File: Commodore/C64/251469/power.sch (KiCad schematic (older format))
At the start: 11 parts, among them CN10 LED Connector, CN7 Power Input, SW1 Power Switch

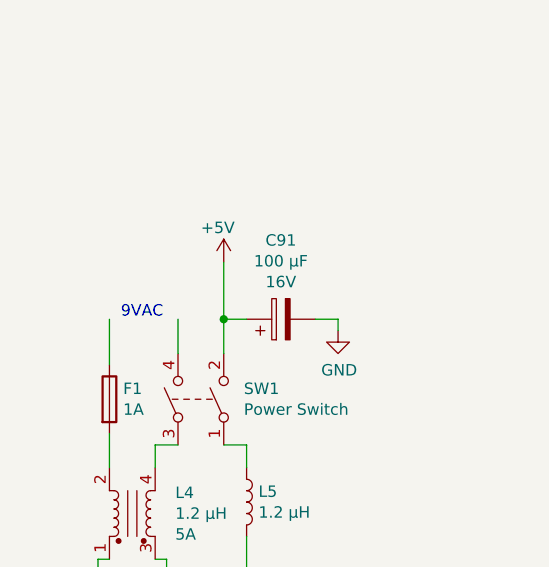
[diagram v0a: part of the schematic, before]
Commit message: Using new 9VAC power symbol
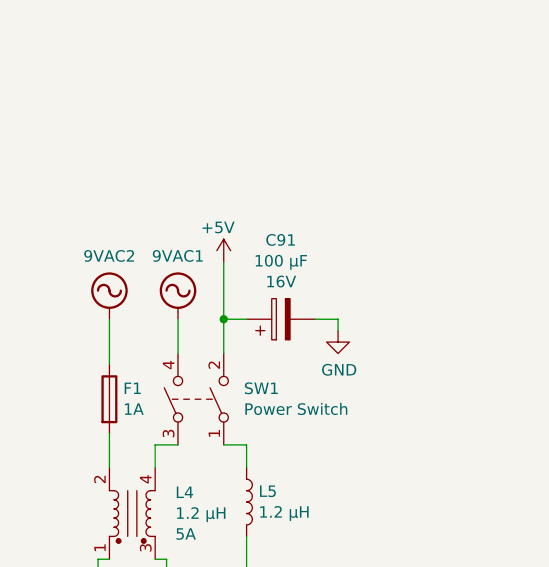
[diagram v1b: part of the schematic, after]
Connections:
- net labels added: 9VAC1, 9VAC2
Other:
- note removed: "9VAC"
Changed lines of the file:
@@
 Wire Wire Line
 	1300 4550 1300 4700
-Text Notes 1050 4550 0    50   ~ 0
-9VAC
+$Comp
+L power_more:9VAC1 #PWR?
+U 1 1 5D2DC784
+P 1300 4550
+F 0 "#PWR?" H 1300 4450 50  0001 C CNN
+F 1 "9VAC1" H 1300 4825 50  0000 C CNN
+F 2 "" H 1300 4550 50  0001 C CNN
+F 3 "" H 1300 4550 50  0001 C CNN
+	1    1300 4550
+	1    0    0    -1
+$EndComp
+$Comp
+L power_more:9VAC2 #PWR?
+U 1 1 5D2DE867
+P 1000 4550
+F 0 "#PWR?" H 1000 4450 50  0001 C CNN
+F 1 "9VAC2" H 1000 4825 50  0000 C CNN
+F 2 "" H 1000 4550 50  0001 C CNN
+F 3 "" H 1000 4550 50  0001 C CNN
+	1    1000 4550
+	1    0    0    -1
+$EndComp
 $EndSCHEMATC

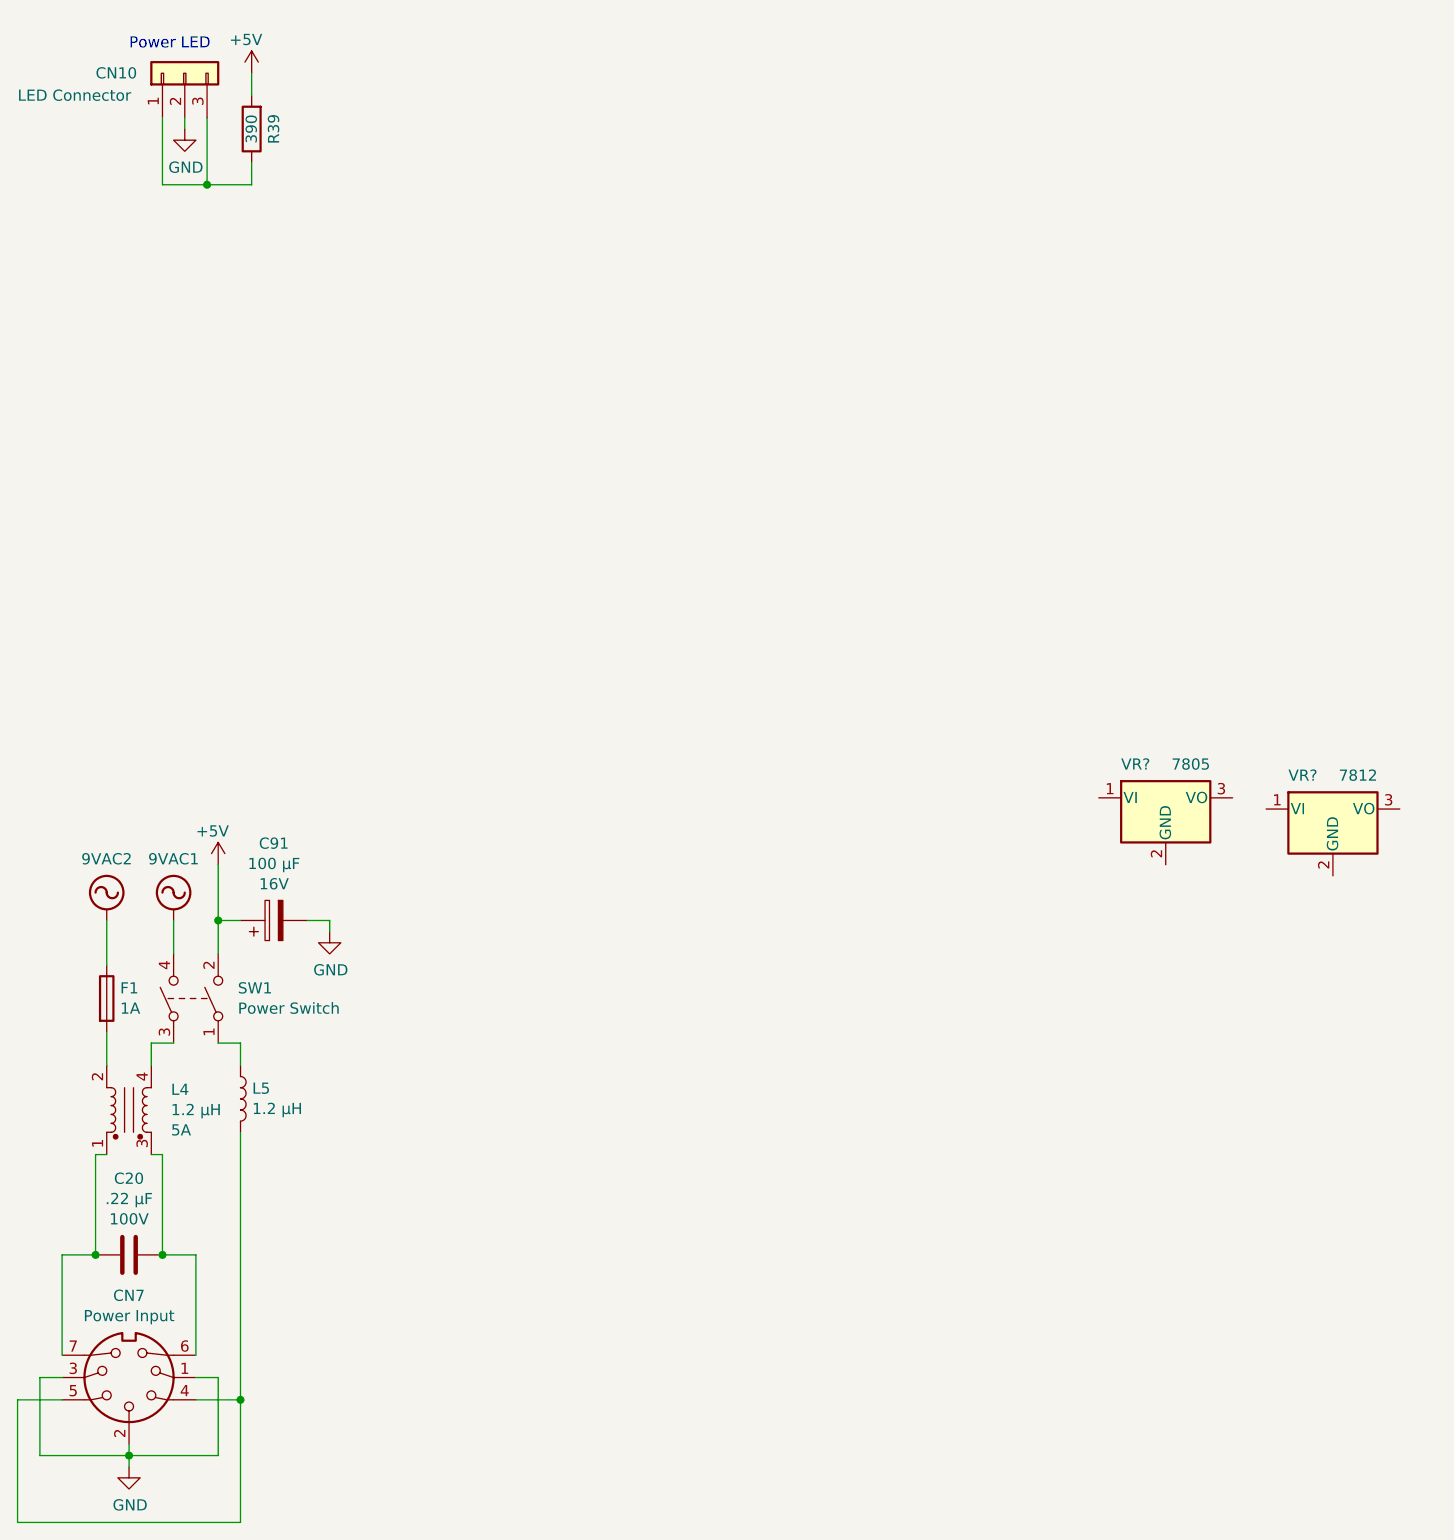
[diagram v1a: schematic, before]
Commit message: CAN+5V regulation circuit added
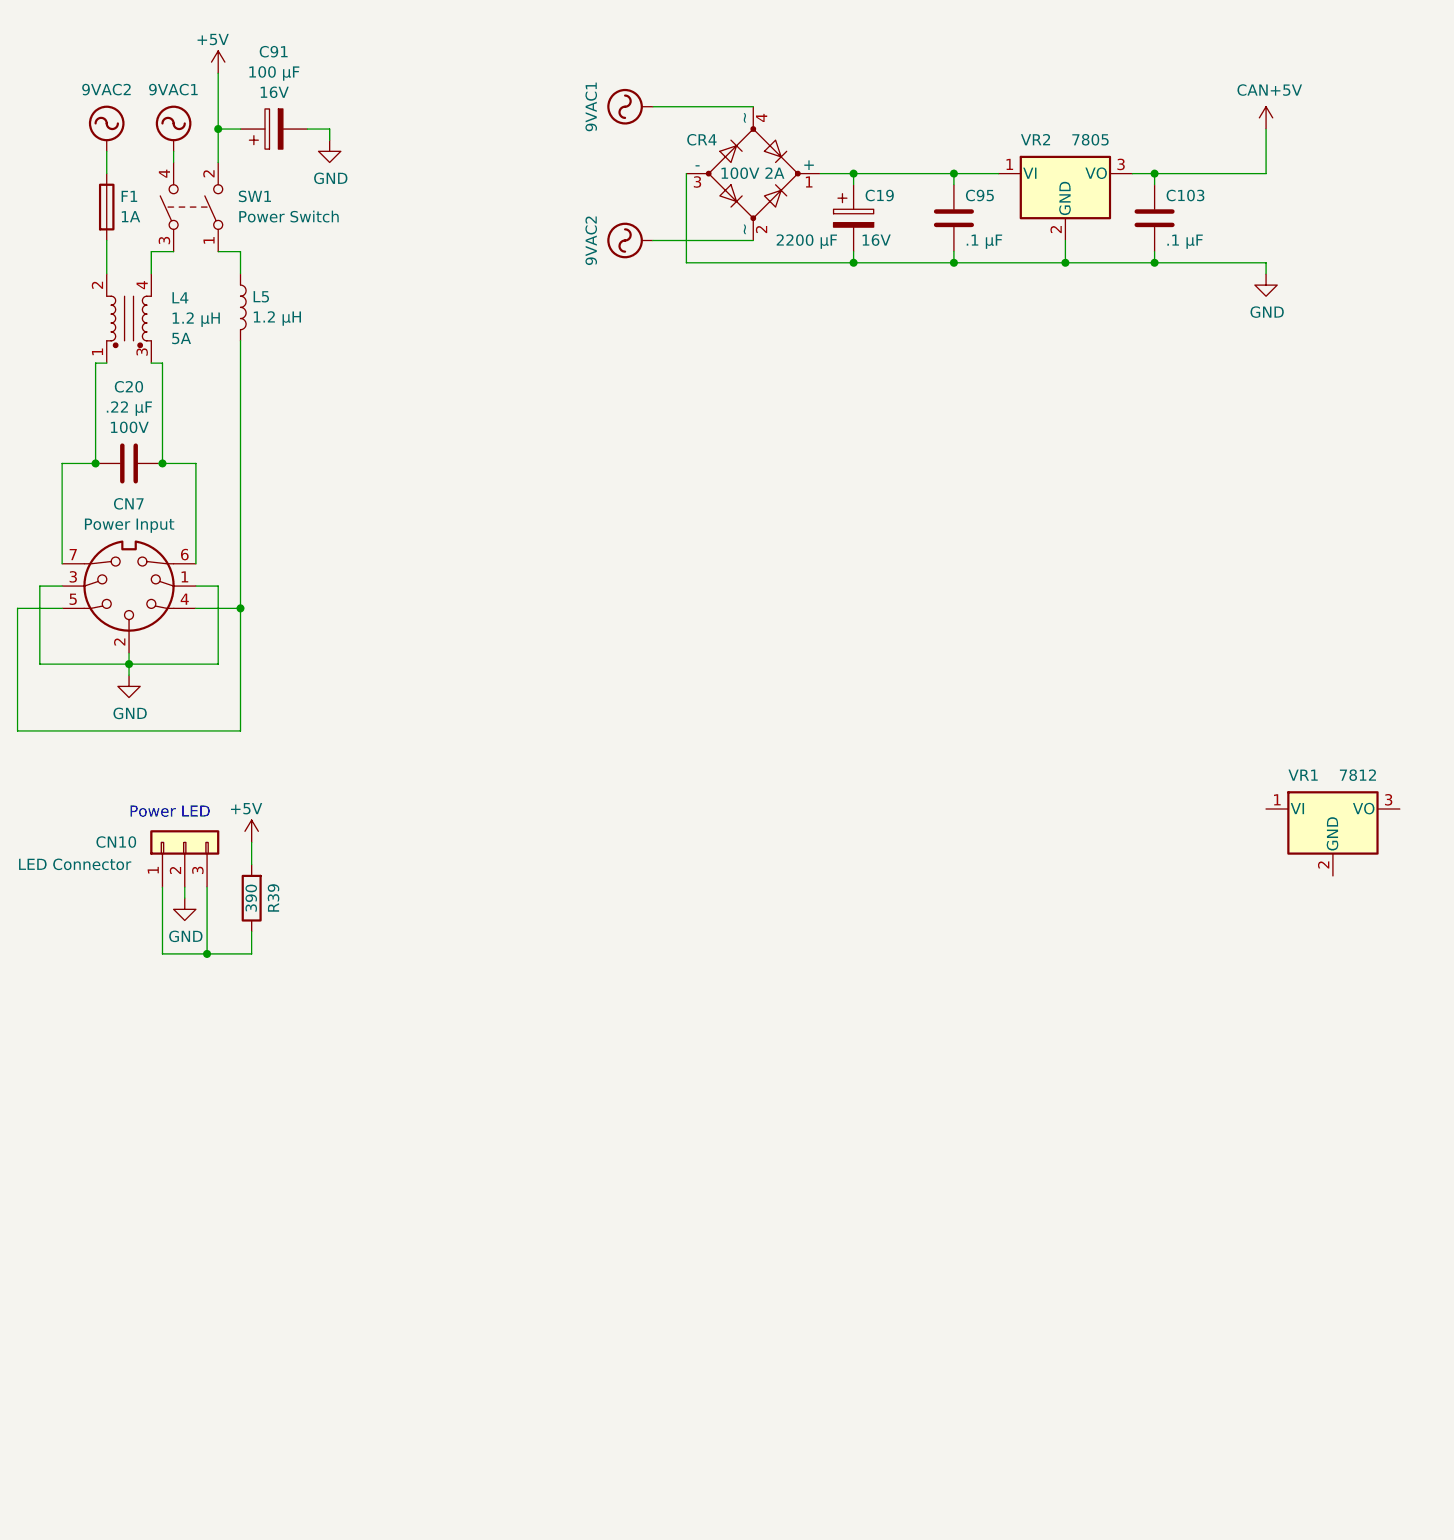
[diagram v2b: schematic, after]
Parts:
- added C103, C95: .1 μF, symbol Device:C
- added C19: 2200 μF, symbol Device:CP
- added CR4: 100V 2A, symbol Device:D_Bridge_+A-A
- gave numbers to parts that had none: 2
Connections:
- net +5V: now also VR2.3 (VO), C103.1
- net GND: now also VR2.2 (GND), C103.2, C19.2, C95.2, CR4.3 (-)
- net VAC: now also CR4.2 (~~), CR4.4 (~~)
- net at VR2.1 (VI): now also C19.1, C95.1, CR4.1 (+)
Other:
- moved on the sheet: C20, C91, CN10, CN7, F1, L4, L5, R39, SW1, VR2

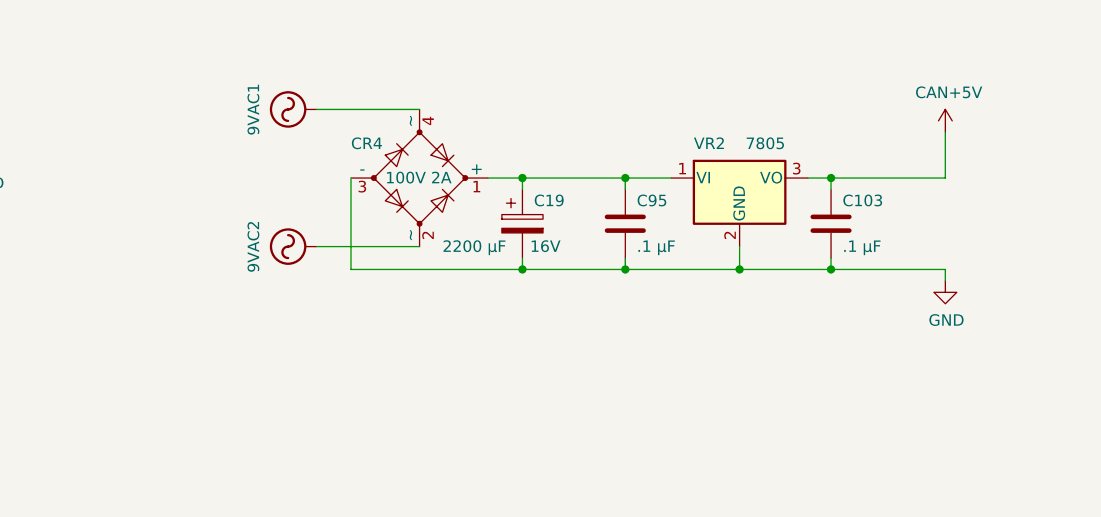
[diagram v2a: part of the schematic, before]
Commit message: UNREG+9V regulation circuit added
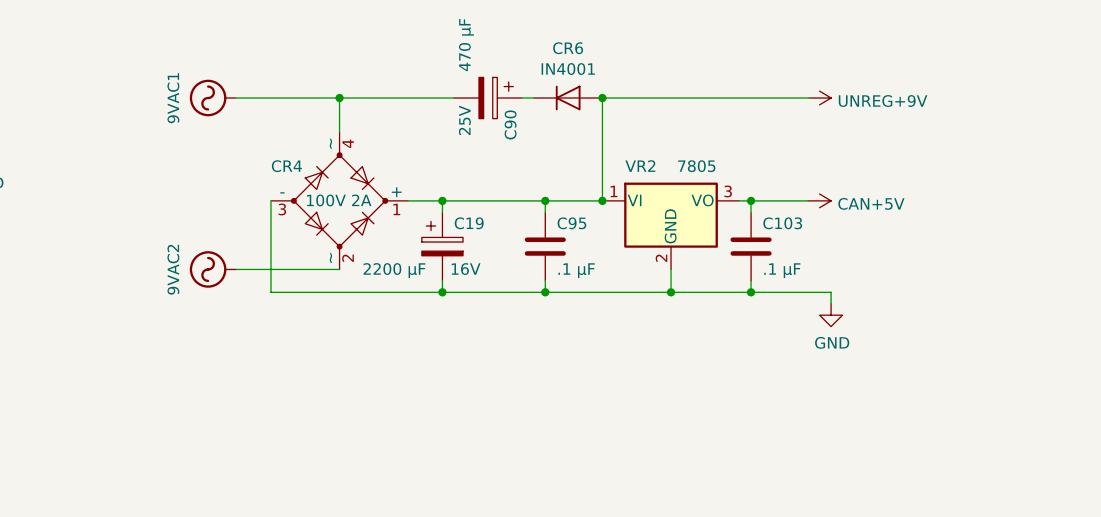
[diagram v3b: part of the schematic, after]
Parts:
- added C90: 470 μF, symbol Device:CP
- added CR6: IN4001, symbol Device:D
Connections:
- net VAC: now also C90.2
- net +9V: now reaches C19.1, C95.1, CR4.1 (+), VR2.1 (VI)
- net +9V: now also CR6.2 (A)
- new net: C90.1, CR6.1 (K)
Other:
- moved on the sheet: C103, C19, C95, CR4, VR2
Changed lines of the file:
@@
 L Regulator_Linear:LM7805_TO220 VR?
 U 1 1 5D95204B
-P 5300 1200
+P 5000 1300
 AR Path="/5D95204B" Ref="VR?"  Part="1"
 AR Path="/5D94F152/5D95204B" Ref="VR2"  Part="1"
-F 0 "VR2" H 5100 1350 50  0000 L CNN
-F 1 "7805" H 5500 1350 50  0000 R CNN
-F 2 "Package_TO_SOT_THT:TO-220-3_Vertical" H 5300 1425 50  0001 C CIN
-F 3 "http://www.fairchildsemi.com/ds/LM/LM7805.pdf" H 5300 1150 50  0001 C CNN
-	1    5300 1200
+F 0 "VR2" H 4800 1450 50  0000 L CNN
+F 1 "7805" H 5200 1450 50  0000 R CNN
+F 2 "Package_TO_SOT_THT:TO-220-3_Vertical" H 5000 1525 50  0001 C CIN
+F 3 "http://www.fairchildsemi.com/ds/LM/LM7805.pdf" H 5000 1250 50  0001 C CNN
+	1    5000 1300
 	1    0    0    -1
 $EndComp
@@
 L Device:D_Bridge_+A-A CR4
 U 1 1 5D30E6B0
-P 3900 1200
-F 0 "CR4" H 3600 1350 50  0000 L CNN
-F 1 "100V 2A" H 3750 1200 50  0000 L CNN
-F 2 "" H 3900 1200 50  0001 C CNN
-F 3 "~" H 3900 1200 50  0001 C CNN
-F 4 "100V" H 4100 1450 50  0001 C CNN "Voltage Rating"
-F 5 "2A" H 4200 1350 50  0001 C CNN "Current Rating"
-	1    3900 1200
+P 3550 1300
+F 0 "CR4" H 3250 1450 50  0000 L CNN
+F 1 "100V 2A" H 3400 1300 50  0000 L CNN
+F 2 "" H 3550 1300 50  0001 C CNN
+F 3 "~" H 3550 1300 50  0001 C CNN
+F 4 "100V" H 3750 1550 50  0001 C CNN "Voltage Rating"
+F 5 "2A" H 3850 1450 50  0001 C CNN "Current Rating"
+	1    3550 1300
 	1    0    0    -1
 $EndComp
@@
 L power_more:9VAC2 #PWR?
 U 1 1 5D30F39C
-P 3450 1500
-F 0 "#PWR?" H 3450 1400 50  0001 C CNN
-F 1 "9VAC2" H 3450 1775 50  0000 C CNN
-F 2 "" H 3450 1500 50  0001 C CNN
-F 3 "" H 3450 1500 50  0001 C CNN
-	1    3450 1500
+P 3100 1600
+F 0 "#PWR?" H 3100 1500 50  0001 C CNN
+F 1 "9VAC2" H 3100 1875 50  0000 C CNN
+F 2 "" H 3100 1600 50  0001 C CNN
+F 3 "" H 3100 1600 50  0001 C CNN
+	1    3100 1600
 	0    -1   -1   0
 $EndComp
@@
 L power_more:9VAC1 #PWR?
 U 1 1 5D30F3A6
-P 3450 900
-F 0 "#PWR?" H 3450 800 50  0001 C CNN
-F 1 "9VAC1" H 3450 1175 50  0000 C CNN
-F 2 "" H 3450 900 50  0001 C CNN
-F 3 "" H 3450 900 50  0001 C CNN
-	1    3450 900
-	0    -1   -1   0
-$EndComp
-Wire Wire Line
-	3900 900  3450 900
-Wire Wire Line
-	3900 1500 3450 1500
-Wire Wire Line
-	3600 1200 3600 1600
-Wire Wire Line
-	3600 1600 4350 1600
+P 3100 850
+F 0 "#PWR?" H 3100 750 50  0001 C CNN
+F 1 "9VAC1" H 3100 1125 50  0000 C CNN
+F 2 "" H 3100 850 50  0001 C CNN
+F 3 "" H 3100 850 50  0001 C CNN
+	1    3100 850
+	0    -1   -1   0
+$EndComp
+Wire Wire Line
+	3250 1300 3250 1700
+Wire Wire Line
+	3250 1700 4000 1700
 $Comp
 L Device:CP C19
 U 1 1 5D319DAB
-P 4350 1400
-F 0 "C19" H 4400 1500 50  0000 L CNN
-F 1 "2200 μF" H 4000 1300 50  0000 L CNN
-F 2 "" H 4388 1250 50  0001 C CNN
-F 3 "~" H 4350 1400 50  0001 C CNN
-F 4 "16V" H 4450 1300 50  0000 C CNN "Voltage Rating"
-	1    4350 1400
-	1    0    0    -1
-$EndComp
-Wire Wire Line
-	4350 1550 4350 1600
-Connection ~ 4350 1600
-Wire Wire Line
-	4350 1600 4800 1600
-Wire Wire Line
-	4200 1200 4350 1200
-Wire Wire Line
-	4350 1250 4350 1200
-Connection ~ 4350 1200
-Wire Wire Line
-	4350 1200 4800 1200
-Wire Wire Line
-	4800 1600 4800 1550
-Wire Wire Line
-	4800 1250 4800 1200
+P 4000 1500
+F 0 "C19" H 4050 1600 50  0000 L CNN
+F 1 "2200 μF" H 3650 1400 50  0000 L CNN
+F 2 "" H 4038 1350 50  0001 C CNN
+F 3 "~" H 4000 1500 50  0001 C CNN
+F 4 "16V" H 4100 1400 50  0000 C CNN "Voltage Rating"
+	1    4000 1500
+	1    0    0    -1
+$EndComp
+Wire Wire Line
+	4000 1650 4000 1700
+Connection ~ 4000 1700
+Wire Wire Line
+	4000 1700 4450 1700
+Wire Wire Line
+	3850 1300 4000 1300
+Wire Wire Line
+	4000 1350 4000 1300
+Connection ~ 4000 1300
+Wire Wire Line
+	4000 1300 4450 1300
+Wire Wire Line
+	4450 1700 4450 1650
+Wire Wire Line
+	4450 1350 4450 1300
 $Comp
 L Device:C C95
 U 1 1 5D31967E
-P 4800 1400
-F 0 "C95" H 4850 1500 50  0000 L CNN
-F 1 ".1 μF" H 4850 1300 50  0000 L CNN
-F 2 "" H 4838 1250 50  0001 C CNN
-F 3 "~" H 4800 1400 50  0001 C CNN
-	1    4800 1400
-	1    0    0    -1
-$EndComp
-Wire Wire Line
-	5000 1200 4800 1200
-Connection ~ 4800 1200
-Wire Wire Line
-	4800 1600 5300 1600
-Wire Wire Line
-	5300 1600 5300 1500
-Connection ~ 4800 1600
-Wire Wire Line
-	5300 1600 5700 1600
-Connection ~ 5300 1600
-Wire Wire Line
-	5600 1200 5700 1200
+P 4450 1500
+F 0 "C95" H 4500 1600 50  0000 L CNN
+F 1 ".1 μF" H 4500 1400 50  0000 L CNN
+F 2 "" H 4488 1350 50  0001 C CNN
+F 3 "~" H 4450 1500 50  0001 C CNN
+	1    4450 1500
+	1    0    0    -1
+$EndComp
+Wire Wire Line
+	4700 1300 4450 1300
+Connection ~ 4450 1300
+Wire Wire Line
+	4450 1700 5000 1700
+Wire Wire Line
+	5000 1700 5000 1600
+Connection ~ 4450 1700
+Wire Wire Line
+	5000 1700 5350 1700
+Connection ~ 5000 1700
+Wire Wire Line
+	5300 1300 5350 1300
 $Comp
 L Device:C C103
 U 1 1 5D334D2E
-P 5700 1400
-F 0 "C103" H 5750 1500 50  0000 L CNN
-F 1 ".1 μF" H 5750 1300 50  0000 L CNN
-F 2 "" H 5738 1250 50  0001 C CNN
-F 3 "~" H 5700 1400 50  0001 C CNN
-	1    5700 1400
-	1    0    0    -1
-$EndComp
-Wire Wire Line
-	5700 1550 5700 1600
-Connection ~ 5700 1600
-Wire Wire Line
-	5700 1600 6200 1600
-Wire Wire Line
-	5700 1250 5700 1200
-Connection ~ 5700 1200
-Wire Wire Line
-	5700 1200 6200 1200
+P 5350 1500
+F 0 "C103" H 5400 1600 50  0000 L CNN
+F 1 ".1 μF" H 5400 1400 50  0000 L CNN
+F 2 "" H 5388 1350 50  0001 C CNN
+F 3 "~" H 5350 1500 50  0001 C CNN
+	1    5350 1500
+	1    0    0    -1
+$EndComp
+Wire Wire Line
+	5350 1650 5350 1700
+Connection ~ 5350 1700
+Wire Wire Line
+	5350 1700 5700 1700
+Wire Wire Line
+	5350 1350 5350 1300
+Connection ~ 5350 1300
+Wire Wire Line
+	5350 1300 5600 1300
 $Comp
 L power_more:CAN+5V #PWR?
 U 1 1 5D33A592
-P 6200 1000
-F 0 "#PWR?" H 6200 850 50  0001 C CNN
-F 1 "CAN+5V" H 6215 1173 50  0000 C CNN
-F 2 "" H 6200 1000 50  0001 C CNN
-F 3 "" H 6200 1000 50  0001 C CNN
-	1    6200 1000
-	1    0    0    -1
-$EndComp
-Wire Wire Line
-	6200 1000 6200 1200
+P 5600 1300
+F 0 "#PWR?" H 5600 1150 50  0001 C CNN
+F 1 "CAN+5V" V 5615 1428 50  0000 L CNN
+F 2 "" H 5600 1300 50  0001 C CNN
+F 3 "" H 5600 1300 50  0001 C CNN
+	1    5600 1300
+	0    1    1    0
+$EndComp
 $Comp
 L power:GND #PWR?
 U 1 1 5D33C4C0
-P 6200 1650
+P 5700 1750
 AR Path="/5D33C4C0" Ref="#PWR?"  Part="1"
 AR Path="/5D94F152/5D33C4C0" Ref="#PWR?"  Part="1"
-F 0 "#PWR?" H 6200 1400 50  0001 C CNN
-F 1 "GND" H 6205 1477 50  0000 C CNN
-F 2 "" H 6200 1650 50  0001 C CNN
-F 3 "" H 6200 1650 50  0001 C CNN
-	1    6200 1650
-	1    0    0    -1
-$EndComp
-Wire Wire Line
-	6200 1650 6200 1600
+F 0 "#PWR?" H 5700 1500 50  0001 C CNN
+F 1 "GND" H 5705 1577 50  0000 C CNN
+F 2 "" H 5700 1750 50  0001 C CNN
+F 3 "" H 5700 1750 50  0001 C CNN
+	1    5700 1750
+	1    0    0    -1
+$EndComp
+Wire Wire Line
+	5700 1750 5700 1700
+$Comp
+L Device:CP C90
+U 1 1 5D33F5CB
+P 4200 850
+F 0 "C90" H 4250 950 50  0000 L CNN
+F 1 "470 μF" H 3850 750 50  0000 L CNN
+F 2 "" H 4238 700 50  0001 C CNN
+F 3 "~" H 4200 850 50  0001 C CNN
+F 4 "25V" H 4300 750 50  0000 C CNN "Voltage Rating"
+	1    4200 850
+	0    1    1    0
+$EndComp
+$Comp
+L Device:D CR6
+U 1 1 5D340F12
+P 4550 850
+F 0 "CR6" H 4550 1066 50  0000 C CNN
+F 1 "IN4001" H 4550 975 50  0000 C CNN
+F 2 "" H 4550 850 50  0001 C CNN
+F 3 "~" H 4550 850 50  0001 C CNN
+	1    4550 850
+	1    0    0    -1
+$EndComp
+Wire Wire Line
+	4350 850  4400 850
+$Comp
+L power_more:UNREG+9V #PWR?
+U 1 1 5D34FA27
+P 5600 850
+F 0 "#PWR?" H 5600 700 50  0001 C CNN
+F 1 "UNREG+9V" V 5615 978 50  0000 L CNN
+F 2 "" H 5600 850 50  0001 C CNN
+F 3 "" H 5600 850 50  0001 C CNN
+	1    5600 850
+	0    1    1    0
+$EndComp
+Wire Wire Line
+	4700 850  4700 1300
+Connection ~ 4700 1300
+Wire Wire Line
+	3550 1000 3550 850
+Wire Wire Line
+	3550 850  3100 850
+Wire Wire Line
+	3550 850  4050 850
+Connection ~ 3550 850
+Wire Wire Line
+	3550 1600 3100 1600
+Connection ~ 4700 850
+Wire Wire Line
+	4700 850  5600 850
 $EndSCHEMATC
